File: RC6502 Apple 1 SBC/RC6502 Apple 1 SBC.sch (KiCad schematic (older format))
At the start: 48 parts, among them J1 VP GND, J10 RAM_EN, J11 PIA_EN, J2 Arduino Nano, J3 Backplane, J4 Hole, J5 Hole, J6 Hole, J7 Hole, J8 Power, J9 ROM_EN, SW1 RESET, U1 WD65C02, U2 HM62256BLP-7, U3 74HCT138, U4 28C256, U5 74HCT00, U6 NE555, U7 74HCT04, U8 WD65C21, U9 MCP23S17, X1 1MHz

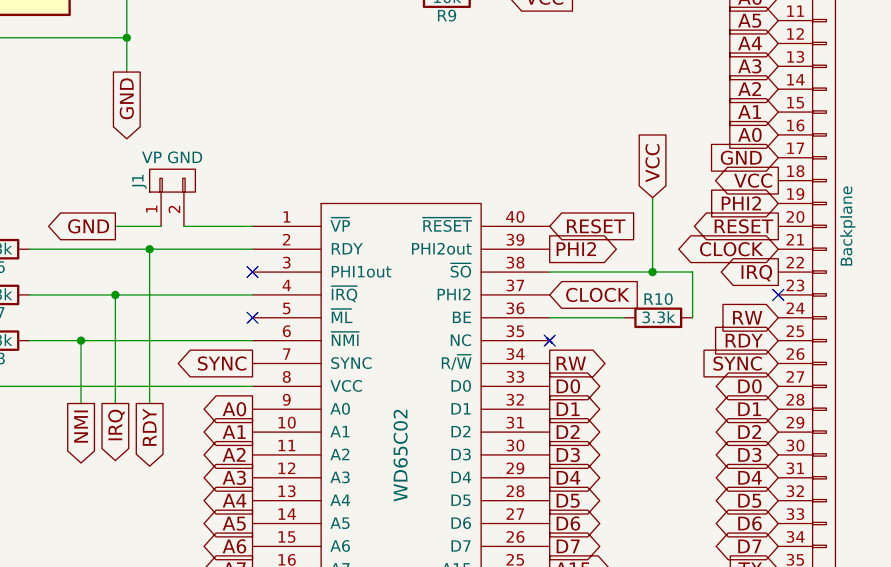
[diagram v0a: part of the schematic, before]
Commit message: Added Phi1 to backplane connector
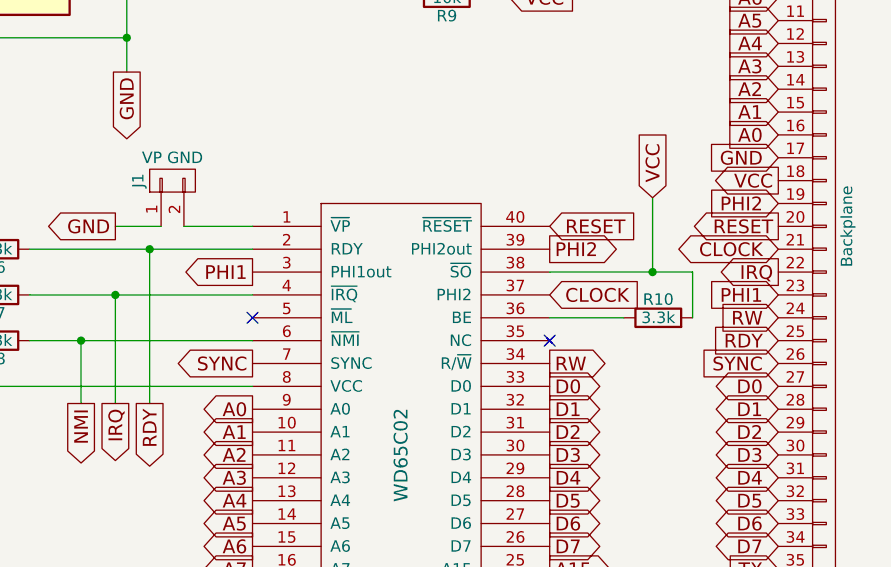
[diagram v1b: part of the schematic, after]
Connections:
- net PHI1: now reaches U1.3 (PHI1out)
- net PHI1: now also J3.23 (P23)
- no-connect marks 42 -> 40
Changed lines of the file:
@@
 Wire Wire Line
 	7500 4650 8475 4650
-NoConn ~ 8475 4550
 Text GLabel 3100 3825 2    60   Input ~ 0
 D0
@@
 Text GLabel 10775 6050 0    60   Input ~ 0
 NMI
-NoConn ~ 10775 4650
 Text GLabel 10775 4850 0    60   Input ~ 0
 RDY
@@
 Wire Wire Line
 	1400 6600 1325 6600
+Text GLabel 10775 4650 0    60   Input ~ 0
+PHI1
+Text GLabel 8475 4550 0    60   Output ~ 0
+PHI1
 $EndSCHEMATC

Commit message: Cleaned up SBC schematic
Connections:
- net CLOCK: now also J2.9 (D6/AIN0)
- no-connect marks 40 -> 39
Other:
- moved on the sheet: A13, A14, C1, C10, C11, C12, C2, C3, C4, C5, C6, C7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

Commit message: Cleaned up SBC schematic some more
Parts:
- J3: symbol CONN_01X39 -> RC6502_Backplane
- U1: value WD65C02 -> 6502; symbol WD65C02 -> 6502
- U8: value WD65C21 -> 6821; symbol WD65C21 -> MC6821
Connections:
- no-connect marks 39 -> 37
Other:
- note added: "Single-board computer (SBC) version of the Apple-1 computer, this version integrates all\nof the core features onto one board (it can still be built using separate modules by\ndisabling the corresponding one here). Originally built while reading the book "Apple-1\nReplica creation" by Tom Owad."
- note added: "These select 8K window within the 32K 28C256, you\ncan also use 28C64 with these selecttions unjumpered."
- moved on the sheet: A13, A14, C12, D1, J1, J10, J11, J2, J8, J9, R1, R10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
